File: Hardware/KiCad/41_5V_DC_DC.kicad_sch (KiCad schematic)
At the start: 0 parts

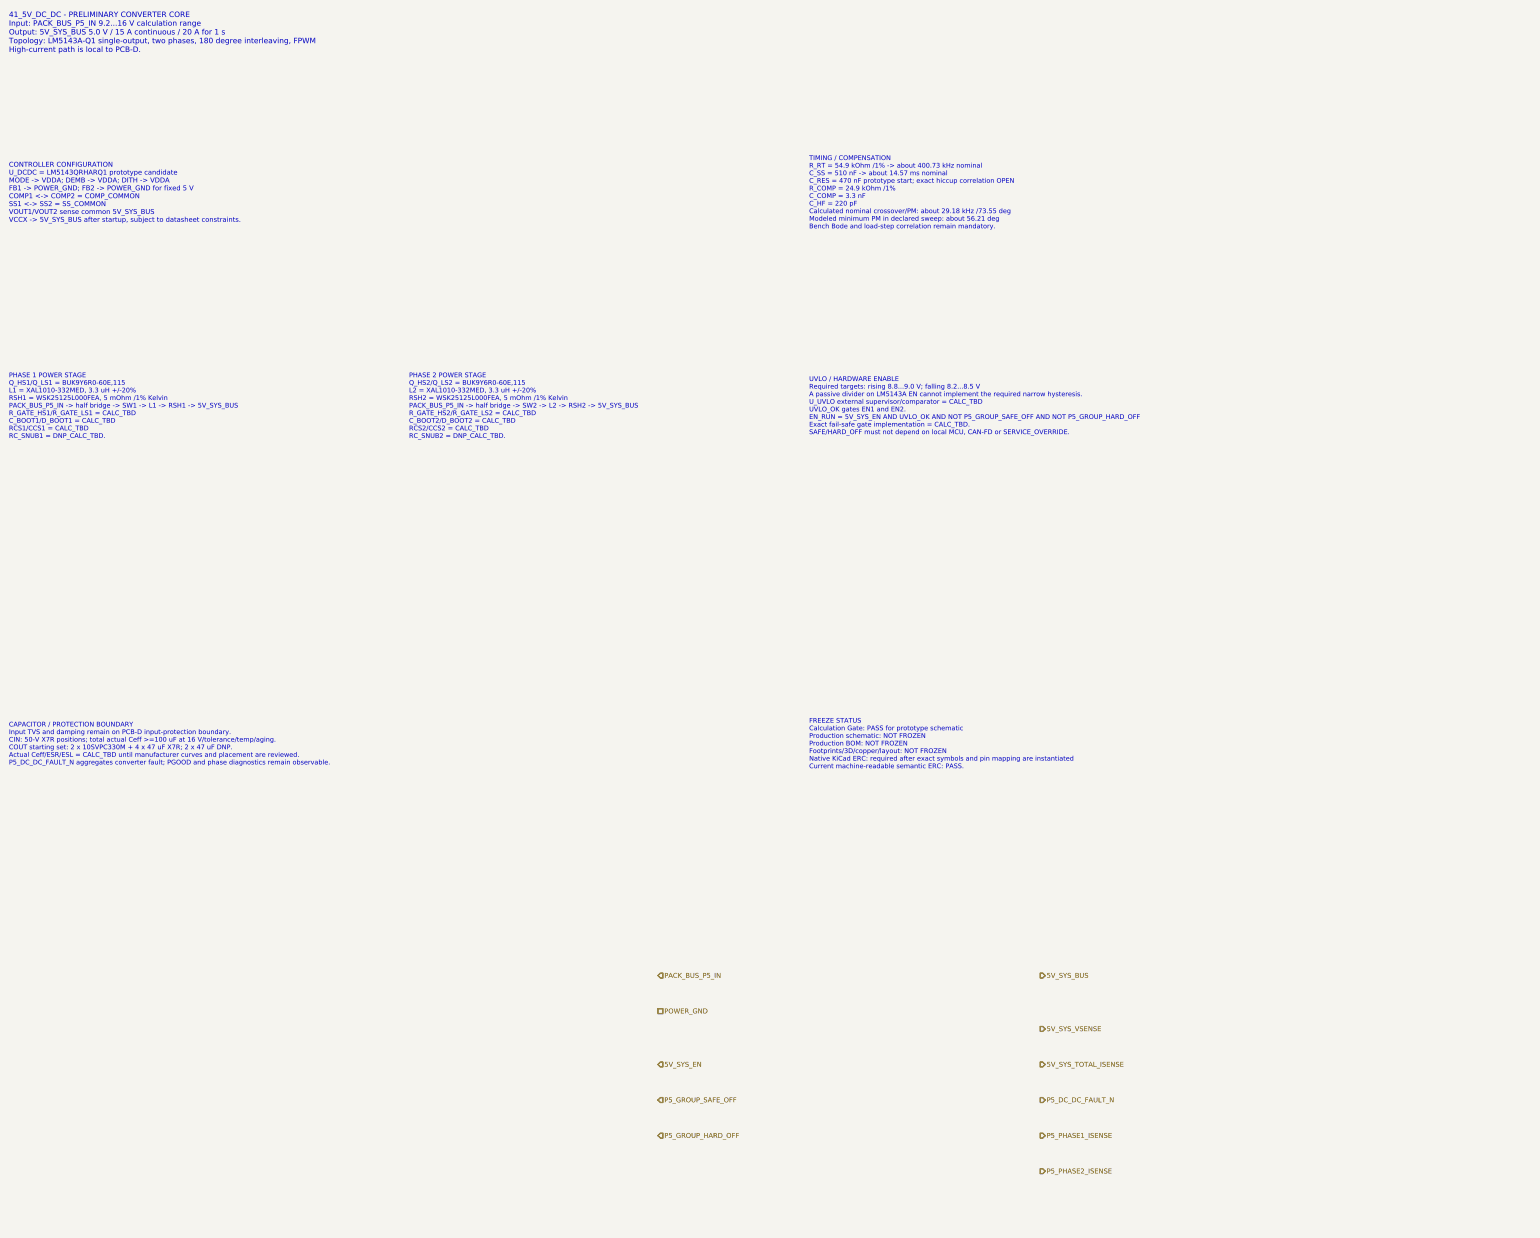
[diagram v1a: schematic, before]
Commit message: hardware: apply LM5143A-Q1 exact pin-map contract V1.9
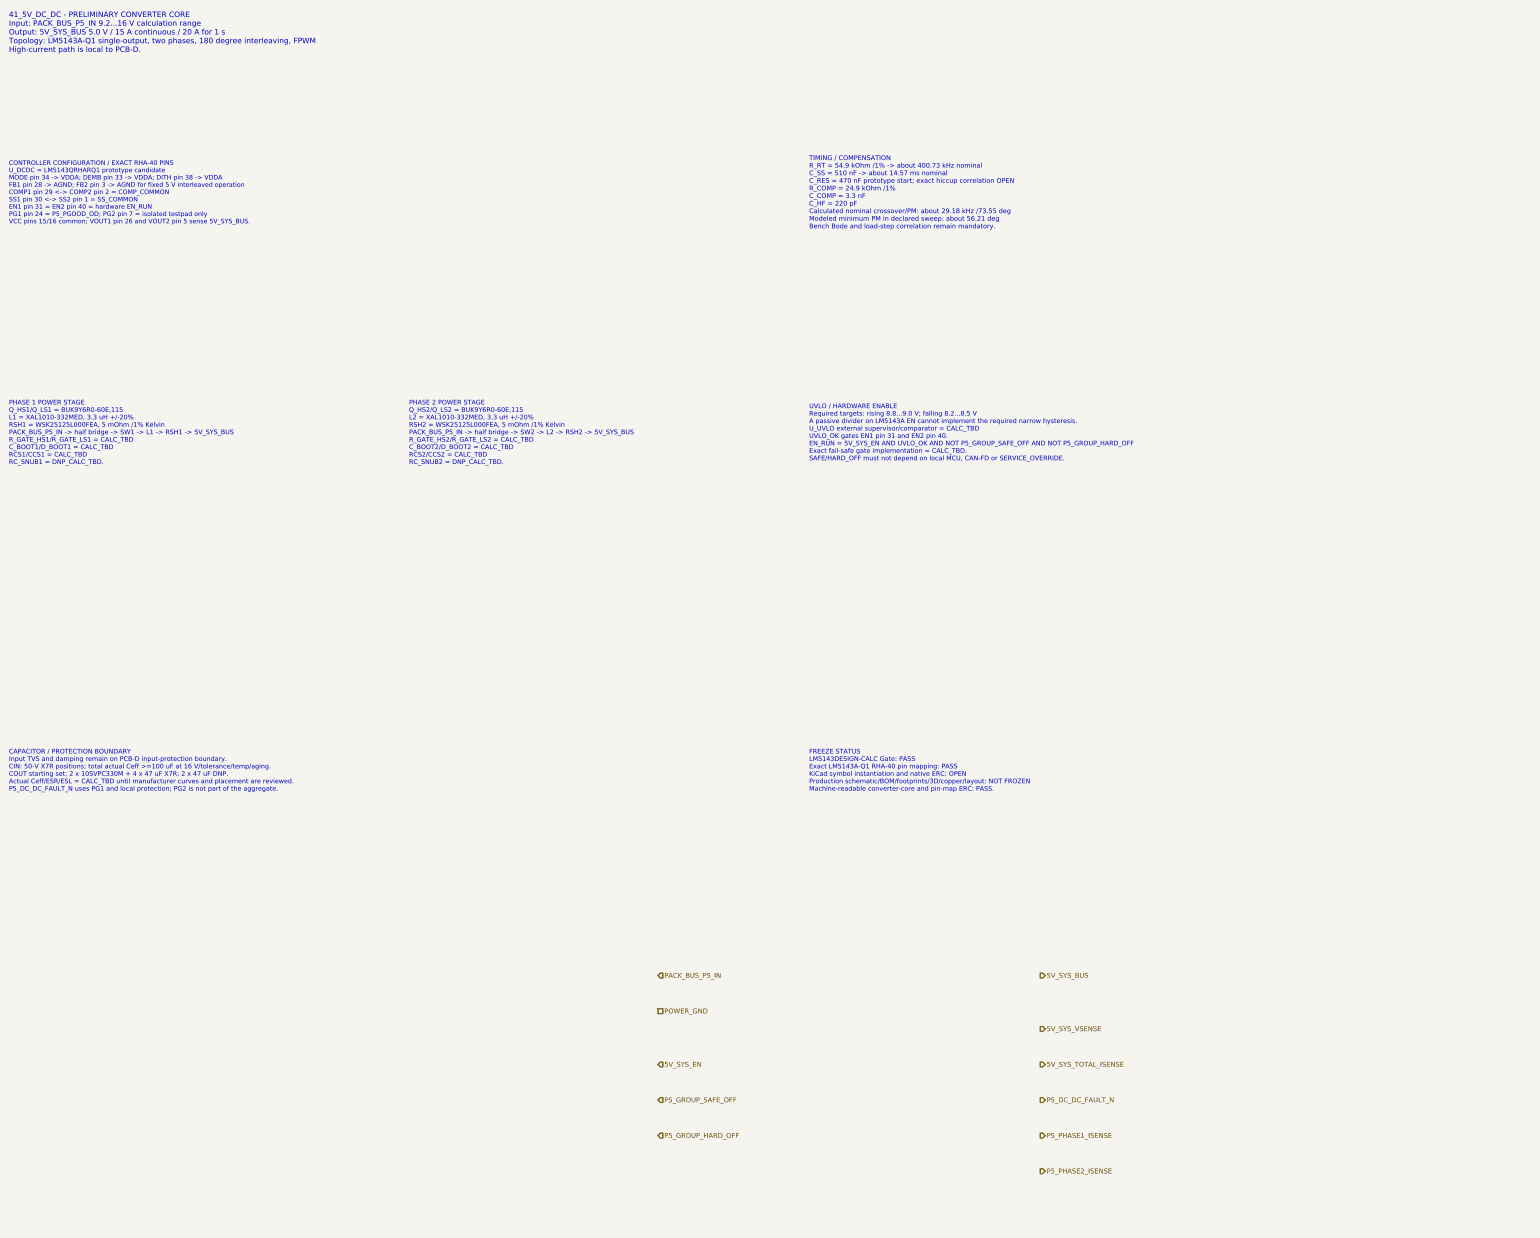
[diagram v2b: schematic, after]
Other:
- note added: "CAPACITOR / PROTECTION BOUNDARY Input TVS and damping remain on PCB-D input-protection boundary. CIN: 50-V X7R positions; total actual Ceff >=100 uF at 16 V/tolerance/temp/aging. COUT starting set: 2 x 10SVPC330M + 4 x 47 uF X7R; 2 x 47 uF DNP. Actual Ceff/ESR/ESL = CALC_TBD until manufacturer curves and placement are reviewed. P5_DC_DC_FAULT_N uses PG1 and local protection; PG2 is not part of th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"
- note added: "CONTROLLER CONFIGURATION / EXACT RHA-40 PINS U_DCDC = LM5143QRHARQ1 prototype candidate MODE pin 34 -> VDDA; DEMB pin 33 -> VDDA; DITH pin 38 -> VDDA FB1 pin 28 -> AGND; FB2 pin 3 -> AGND for fixed 5 V interleaved operation COMP1 pin 29 <-> COMP2 pin 2 = COMP_COMMON SS1 pin 30 <-> SS2 pin 1 = SS_COMMON EN1 pin 31 = EN2 pin 40 = hardware EN_RUN PG1 pin 24 = P5_PGOOD_OD; PG2 pin 7 = isolated testpa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"
- note added: "FREEZE STATUS LM5143DESIGN-CALC Gate: PASS Exact LM5143A-Q1 RHA-40 pin mapping: PASS KiCad symbol instantiation and native ERC: OPEN Production schematic/BOM/footprints/3D/copper/layout: NOT FROZEN Machine-readable converter-core and pin-map ERC: PASS."
- note added: "UVLO / HARDWARE ENABLE Required targets: rising 8.8...9.0 V; falling 8.2...8.5 V A passive divider on LM5143A EN cannot implement the required narrow hysteresis. U_UVLO external supervisor/comparator = CALC_TBD UVLO_OK gates EN1 pin 31 and EN2 pin 40. EN_RUN = 5V_SYS_EN AND UVLO_OK AND NOT P5_GROUP_SAFE_OFF AND NOT P5_GROUP_HARD_OFF Exact fail-safe gate implementation = CALC_TBD. SAFE/HARD_OFF mu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"
- note removed: "CAPACITOR / PROTECTION BOUNDARY Input TVS and damping remain on PCB-D input-protection boundary. CIN: 50-V X7R positions; total actual Ceff >=100 uF at 16 V/tolerance/temp/aging. COUT starting set: 2 x 10SVPC330M + 4 x 47 uF X7R; 2 x 47 uF DNP. Actual Ceff/ESR/ESL = CALC_TBD until manufacturer curves and placement are reviewed. P5_DC_DC_FAULT_N aggregates converter fault; PGOOD and phase diagnost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"
- note removed: "CONTROLLER CONFIGURATION U_DCDC = LM5143QRHARQ1 prototype candidate MODE -> VDDA; DEMB -> VDDA; DITH -> VDDA FB1 -> POWER_GND; FB2 -> POWER_GND for fixed 5 V COMP1 <-> COMP2 = COMP_COMMON SS1 <-> SS2 = SS_COMMON VOUT1/VOUT2 sense common 5V_SYS_BUS VCCX -> 5V_SYS_BUS after startup, subject to datasheet constraints."
- note removed: "FREEZE STATUS Calculation Gate: PASS for prototype schematic Production schematic: NOT FROZEN Production BOM: NOT FROZEN Footprints/3D/copper/layout: NOT FROZEN Native KiCad ERC: required after exact symbols and pin mapping are instantiated Current machine-readable semantic ERC: PASS."
- note removed: "UVLO / HARDWARE ENABLE Required targets: rising 8.8...9.0 V; falling 8.2...8.5 V A passive divider on LM5143A EN cannot implement the required narrow hysteresis. U_UVLO external supervisor/comparator = CALC_TBD UVLO_OK gates EN1 and EN2. EN_RUN = 5V_SYS_EN AND UVLO_OK AND NOT P5_GROUP_SAFE_OFF AND NOT P5_GROUP_HARD_OFF Exact fail-safe gate implementation = CALC_TBD. SAFE/HARD_OFF must not depend 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"
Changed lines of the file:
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@@
 	(title_block
 		(title "41_5V_DC_DC - PCB-D converter core V1.9")
-		(date "2026-07-21")
-		(rev "B1-CALC")
+		(date "2026-07-23")
+		(rev "B2-PINMAP")
 		(company "Gonoboben/plataVM")
-		(comment 1 "Prototype converter-core definition after LM5143DESIGN-CALC Gate")
-		(comment 2 "CALC_TBD values explicit; no production BOM, footprints, copper or layout freeze")
+		(comment 1 "Prototype converter-core definition after LM5143DESIGN-CALC and exact RHA-40 pin-map Gates")
+		(comment 2 "Pin map verified; symbol instantiation/native ERC open; no production BOM, footprint, copper or layout freeze")
 	)
 	(text "41_5V_DC_DC - PRELIMINARY CONVERTER CORE\nInput: PACK_BUS_P5_IN 9.2...16 V calculation range\nOutput: 5V_SYS_BUS 5.0 V / 15 A continuous / 20 A for 1 s\nTopology: LM5143A-Q1 single-output, two phases, 180 degree interleaving, FPWM\nHigh-current path is local to PCB-D."
@@
 		(uuid "power-5v-00000041-0000-4000-8000-000000000101")
 	)
-	(text "CONTROLLER CONFIGURATION\nU_DCDC = LM5143QRHARQ1 prototype candidate\nMODE -> VDDA; DEMB -> VDDA; DITH -> VDDA\nFB1 -> POWER_GND; FB2 -> POWER_GND for fixed 5 V\nCOMP1 <-> COMP2 = COMP_COMMON\nSS1 <-> SS2 = SS_COMMON\nVOUT1/VOUT2 sense common 5V_SYS_BUS\nVCCX -> 5V_SYS_BUS after startup, subject to datasheet constraints."
+	(text "CONTROLLER CONFIGURATION / EXACT RHA-40 PINS\nU_DCDC = LM5143QRHARQ1 prototype candidate\nMODE pin 34 -> VDDA; DEMB pin 33 -> VDDA; DITH pin 38 -> VDDA\nFB1 pin 28 -> AGND; FB2 pin 3 -> AGND for fixed 5 V interleaved operation\nCOMP1 pin 29 <-> COMP2 pin 2 = COMP_COMMON\nSS1 pin 30 <-> SS2 pin 1 = SS_COMMON\nEN1 pin 31 = EN2 pin 40 = hardware EN_RUN\nPG1 pin 24 = P5_PGOOD_OD; PG2 pin 7 = isolated testpad only\nVCC pins 15/16 common; VOUT1 pin 26 and VOUT2 pin 5 sense 5V_SYS_BUS."
 		(exclude_from_sim no)
 		(at 12 48 0)
-		(effects (font (size 1.10 1.10)) (justify left))
+		(effects (font (size 1.02 1.02)) (justify left))
 		(uuid "power-5v-00000041-0000-4000-8000-000000000102")
 	)
 	(text "PHASE 1 POWER STAGE\nQ_HS1/Q_LS1 = BUK9Y6R0-60E,115\nL1 = XAL1010-332MED, 3.3 uH +/-20%\nRSH1 = WSK25125L000FEA, 5 mOhm /1% Kelvin\nPACK_BUS_P5_IN -> half bridge -> SW1 -> L1 -> RSH1 -> 5V_SYS_BUS\nR_GATE_HS1/R_GATE_LS1 = CALC_TBD\nC_BOOT1/D_BOOT1 = CALC_TBD\nRCS1/CCS1 = CALC_TBD\nRC_SNUB1 = DNP_CALC_TBD."
 		(exclude_from_sim no)
-		(at 12 96 0)
-		(effects (font (size 1.06 1.06)) (justify left))
+		(at 12 102 0)
+		(effects (font (size 1.04 1.04)) (justify left))
 		(uuid "power-5v-00000041-0000-4000-8000-000000000103")
 	)
 	(text "PHASE 2 POWER STAGE\nQ_HS2/Q_LS2 = BUK9Y6R0-60E,115\nL2 = XAL1010-332MED, 3.3 uH +/-20%\nRSH2 = WSK25125L000FEA, 5 mOhm /1% Kelvin\nPACK_BUS_P5_IN -> half bridge -> SW2 -> L2 -> RSH2 -> 5V_SYS_BUS\nR_GATE_HS2/R_GATE_LS2 = CALC_TBD\nC_BOOT2/D_BOOT2 = CALC_TBD\nRCS2/CCS2 = CALC_TBD\nRC_SNUB2 = DNP_CALC_TBD."
 		(exclude_from_sim no)
-		(at 102 96 0)
-		(effects (font (size 1.06 1.06)) (justify left))
+		(at 102 102 0)
+		(effects (font (size 1.04 1.04)) (justify left))
 		(uuid "power-5v-00000041-0000-4000-8000-000000000104")
 	)
@@
 		(uuid "power-5v-00000041-0000-4000-8000-000000000105")
 	)
-	(text "UVLO / HARDWARE ENABLE\nRequired targets: rising 8.8...9.0 V; falling 8.2...8.5 V\nA passive divider on LM5143A EN cannot implement the required narrow hysteresis.\nU_UVLO external supervisor/comparator = CALC_TBD\nUVLO_OK gates EN1 and EN2.\nEN_RUN = 5V_SYS_EN AND UVLO_OK AND NOT P5_GROUP_SAFE_OFF AND NOT P5_GROUP_HARD_OFF\nExact fail-safe gate implementation = CALC_TBD.\nSAFE/HARD_OFF must not depend on local MCU, CAN-FD or SERVICE_OVERRIDE."
+	(text "UVLO / HARDWARE ENABLE\nRequired targets: rising 8.8...9.0 V; falling 8.2...8.5 V\nA passive divider on LM5143A EN cannot implement the required narrow hysteresis.\nU_UVLO external supervisor/comparator = CALC_TBD\nUVLO_OK gates EN1 pin 31 and EN2 pin 40.\nEN_RUN = 5V_SYS_EN AND UVLO_OK AND NOT P5_GROUP_SAFE_OFF AND NOT P5_GROUP_HARD_OFF\nExact fail-safe gate implementation = CALC_TBD.\nSAFE/HARD_OFF must not depend on local MCU, CAN-FD or SERVICE_OVERRIDE."
 		(exclude_from_sim no)
-		(at 192 96 0)
-		(effects (font (size 1.06 1.06)) (justify left))
+		(at 192 102 0)
+		(effects (font (size 1.04 1.04)) (justify left))
 		(uuid "power-5v-00000041-0000-4000-8000-000000000106")
 	)
-	(text "CAPACITOR / PROTECTION BOUNDARY\nInput TVS and damping remain on PCB-D input-protection boundary.\nCIN: 50-V X7R positions; total actual Ceff >=100 uF at 16 V/tolerance/temp/aging.\nCOUT starting set: 2 x 10SVPC330M + 4 x 47 uF X7R; 2 x 47 uF DNP.\nActual Ceff/ESR/ESL = CALC_TBD until manufacturer curves and placement are reviewed.\nP5_DC_DC_FAULT_N aggregates converter fault; PGOOD and phase diagnostics remain observable."
+	(text "CAPACITOR / PROTECTION BOUNDARY\nInput TVS and damping remain on PCB-D input-protection boundary.\nCIN: 50-V X7R positions; total actual Ceff >=100 uF at 16 V/tolerance/temp/aging.\nCOUT starting set: 2 x 10SVPC330M + 4 x 47 uF X7R; 2 x 47 uF DNP.\nActual Ceff/ESR/ESL = CALC_TBD until manufacturer curves and placement are reviewed.\nP5_DC_DC_FAULT_N uses PG1 and local protection; PG2 is not part of the aggregate."
 		(exclude_from_sim no)
-		(at 12 172 0)
-		(effects (font (size 1.06 1.06)) (justify left))
+		(at 12 178 0)
+		(effects (font (size 1.04 1.04)) (justify left))
 		(uuid "power-5v-00000041-0000-4000-8000-000000000107")
 	)
-	(text "FREEZE STATUS\nCalculation Gate: PASS for prototype schematic\nProduction schematic: NOT FROZEN\nProduction BOM: NOT FROZEN\nFootprints/3D/copper/layout: NOT FROZEN\nNative KiCad ERC: required after exact symbols and pin mapping are instantiated\nCurrent machine-readable semantic ERC: PASS."
+	(text "FREEZE STATUS\nLM5143DESIGN-CALC Gate: PASS\nExact LM5143A-Q1 RHA-40 pin mapping: PASS\nKiCad symbol instantiation and native ERC: OPEN\nProduction schematic/BOM/footprints/3D/copper/layout: NOT FROZEN\nMachine-readable converter-core and pin-map ERC: PASS."
 		(exclude_from_sim no)
-		(at 192 172 0)
-		(effects (font (size 1.06 1.06)) (justify left))
+		(at 192 178 0)
+		(effects (font (size 1.04 1.04)) (justify left))
 		(uuid "power-5v-00000041-0000-4000-8000-000000000108")
 	)
